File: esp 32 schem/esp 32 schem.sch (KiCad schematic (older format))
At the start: 22 parts, among them U1 ESP32-WROOM-32, U2 MAX1487E

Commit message: modified uart circuit for stm8 and stm32
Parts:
- removed U?: SMD_2062, symbol Custom_Library:SMD_2062
- added U?: MAX1487E, symbol Interface_UART:MAX1487E
- added U?: SMD_2062, symbol Custom_Library:SMD_2062
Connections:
- net labels added: RX_STM8, TX_STM8, UART_STM8_EN_TX, UART_STM8_TX_EN
- net labels removed: TXRX_STM8
- wire segments 100 -> 107
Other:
- note added: "to stm8 usart\n"
- note removed: "usart transmission to STM8\n"
- moved on the sheet: K?, R?, U?

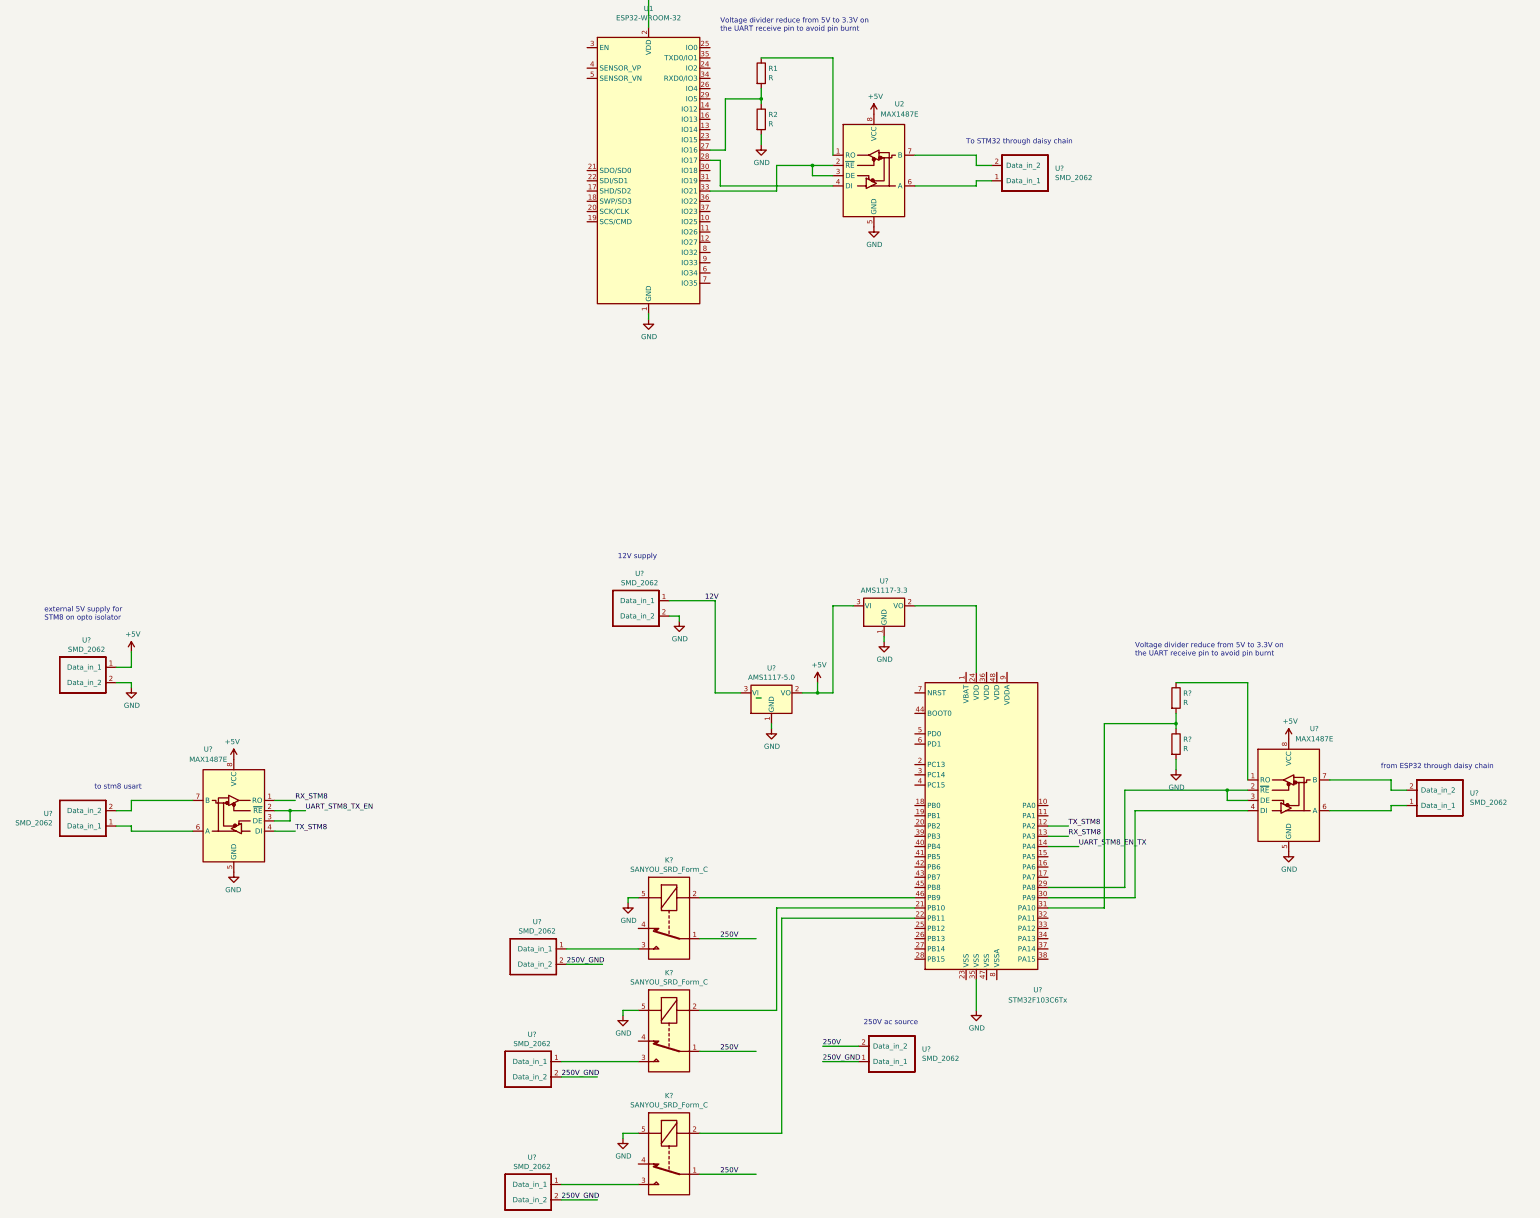
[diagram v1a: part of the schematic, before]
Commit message: updated schematics for stm8 and esp32
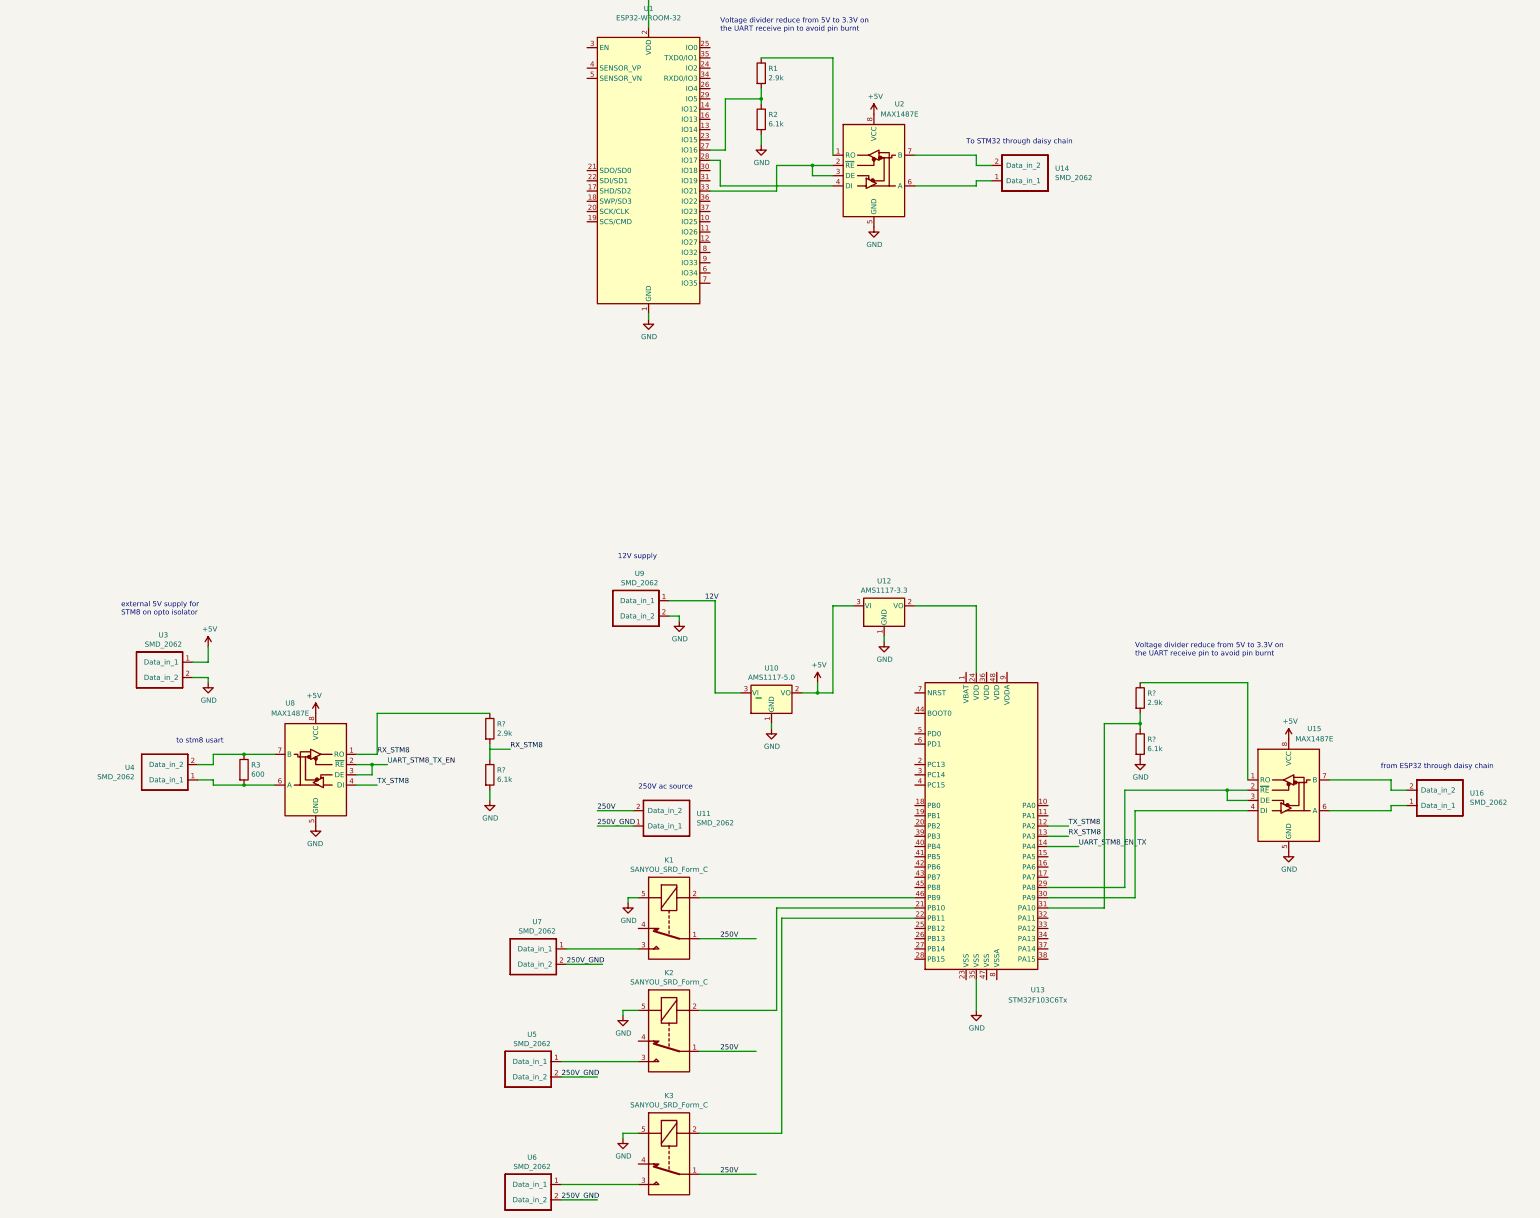
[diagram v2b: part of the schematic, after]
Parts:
- removed R? (x2): R, symbol Device:R
- added R3: 600, symbol Device:R
- added R? (x2): 2.9k, symbol Device:R
- added R? (x2): 6.1k, symbol Device:R
- R1: value R -> 2.9k
- R2: value R -> 6.1k
- gave numbers to parts that had none: 17
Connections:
- wire segments 107 -> 113
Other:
- moved on the sheet: U11, U3, U4, U8
